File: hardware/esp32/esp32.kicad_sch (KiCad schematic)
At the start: 42 parts, among them U1 AMS1117-3.3, U2 ESP32-S3-MINI-1-N8, U3 ESD7104MUTAG, U4 BDR6133, U5 TLV75801PDRV

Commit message: TPS629210DRLR
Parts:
- removed C17, C18: 10u, Capacitor_SMD:C_0603_1608Metric, symbol Device:C
- removed C3: 100nF, Capacitor_SMD:C_0603_1608Metric, symbol Device:C
- removed C6: 10uF, Capacitor_SMD:C_0603_1608Metric, symbol Device:C_Small
- removed R8: 5.1k, Resistor_SMD:R_0603_1608Metric, symbol Device:R_Small
- removed U1: AMS1117-3.3, Package_TO_SOT_SMD:SOT-89-3, symbol Regulator_Linear:AMS1117-3.3
- removed U5: TLV75801PDRV, Package_SON:WSON-6-1EP_2x2mm_P0.65mm_EP1x1.6mm, symbol Regulator_Linear:TLV75801PDRV
- added C2, C3: 10uF, Capacitor_SMD:C_0603_1608Metric, symbol Device:C_Small
- added C5: 22uF, Capacitor_SMD:C_0603_1608Metric, symbol Device:C_Small
- added L1: 2.2uH,50mA, PCM_JLCPCB:L_0805, symbol PCM_JLCPCB-Inductors:2.2uH,50mA
- added R4: 249K, Resistor_SMD:R_0603_1608Metric, symbol Device:R_Small
- added R5: 100K, Resistor_SMD:R_0603_1608Metric, symbol Device:R_Small
- added U1: TPS629210DRLR, TPS629210DRLR:SOT50P160X60-8N, symbol TPS629210DRLR:TPS629210DRLR
- R6: value 1M -> 52.3K
- R7: value 200k -> 1K
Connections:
- net 5VUSB: now also C7.1, D1.1 (+), U4.3 (VM), C2.1, C3.1, U1.6 (VIN), U1.7 (EN)
- net GND: now also R6.1, C2.2, C3.2, C5.2, R4.1, U1.5 (GND); no longer R7.1
- net VCC: now also R7.2, C5.1, L1.2, R5.1, U1.3 (VOS); no longer C7.1, R6.2
- net at D2.2 (A): now also R7.1
- new net: R4.2, U1.1 (FB/VSET)
- new net: R5.2, U1.2 (PG)
- new net: R6.2, U1.8 (MODE/S-CONF)
- new net: L1.1, U1.4 (SW)
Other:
- moved on the sheet: C7, D2, R6, g1, g2, g3, g4

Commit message: jst
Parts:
- removed g1, g2, g3, g4, g5, g6, g7, o1, o10, o2, o3, o4, o5, o6, o7, o8, o9, tr1, tr2: TestPoint, TestPoint:TestPoint_THTPad_1.5x1.5mm_Drill0.7mm, symbol Connector:TestPoint
- added J1, J2, J3: Conn_01x02, Connector_JST:JST_SHL_SM02B-SHLS-TF_1x02-1MP_P1.00mm_Horizontal, symbol Connector_Generic:Conn_01x02
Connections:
- net GND: now also J3.1 (Pin_1), J3.2 (Pin_2)
- net at D1.3: now also J1.1 (Pin_1)
- net at D1.4: now also J1.2 (Pin_2)
- net at U4.4 (OUTA): now also J2.1 (Pin_1)
- net at U4.5 (OUTB): now also J2.2 (Pin_2)

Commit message: wip:  - ldo with ams  - ldo with TPS629210DRLR  - esp32 with usb and connectors  - tlc5940
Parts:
- added J4: Conn_01x06, Connector_JST:JST_SHL_SM06B-SHLS-TF_1x06-1MP_P1.00mm_Horizontal, symbol Connector_Generic:Conn_01x06
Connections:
- net at U2.13 (IO9): now also U4.7 (INB)
- net at U2.14 (IO10): now also U4.6 (INA)
- net at U2.16 (IO12): no longer U4.7 (INB)
- net at U2.17 (IO13): no longer U4.6 (INA)
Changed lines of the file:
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@@
 	(wire
 		(pts
-			(xy 166.37 71.12) (xy 201.93 71.12)
-		)
-		(stroke
-			(width 0)
-			(type default)
-		)
-	)
-	(wire
-		(pts
 			(xy 71.12 30.48) (xy 85.09 30.48)
 		)
@@
 	(wire
 		(pts
-			(xy 196.85 68.58) (xy 196.85 92.71)
+			(xy 196.85 60.96) (xy 196.85 92.71)
 		)
 		(stroke
@@
 	(wire
 		(pts
-			(xy 166.37 13.97) (xy 166.37 71.12)
+			(xy 166.37 13.97) (xy 166.37 63.5)
 		)
 		(stroke
@@
 	(wire
 		(pts
+			(xy 166.37 63.5) (xy 201.93 63.5)
+		)
+		(stroke
+			(width 0)
+			(type default)
+		)
+	)
+	(wire
+		(pts
 			(xy 193.04 38.1) (xy 193.04 46.99)
 		)
@@
 	(wire
 		(pts
+			(xy 196.85 60.96) (xy 201.93 60.96)
+		)
+		(stroke
+			(width 0)
+			(type default)
+		)
+	)
+	(wire
+		(pts
 			(xy 46.99 148.59) (xy 50.8 148.59)
 		)
@@
 	(wire
 		(pts
-			(xy 196.85 68.58) (xy 201.93 68.58)
-		)
-		(stroke
-			(width 0)
-			(type default)
-		)
-	)
-	(wire
-		(pts
 			(xy 50.8 175.26) (xy 48.26 175.26)
 		)
@@
 					(unit 1)
 				)
+			)
+		)
+	)
+	(symbol
+		(lib_id "Connector_Generic:Conn_01x06")
+		(at 166.37 114.3 0)
+		(unit 1)
+		(exclude_from_sim no)
+		(in_bom yes)
+		(on_board yes)
+		(dnp no)
+		(fields_autoplaced yes)
+		(property "Reference" "J4"
+			(at 168.91 114.2999 0)
+			(effects
+				(font
+					(size 1.27 1.27)
+				)
+				(justify left)
+			)
+		)
+		(property "Value" "Conn_01x06"
+			(at 168.91 116.8399 0)
+			(effects
+				(font
+					(size 1.27 1.27)
+				)
+				(justify left)
+			)
+		)
+		(property "Footprint" "Connector_JST:JST_SHL_SM06B-SHLS-TF_1x06-1MP_P1.00mm_Horizontal"
+			(at 166.37 114.3 0)
+			(effects
+				(font
+					(size 1.27 1.27)
+				)
+				(hide yes)
+			)
+		)
+		(property "Datasheet" "~"
+			(at 166.37 114.3 0)
+			(effects
+				(font
+					(size 1.27 1.27)
+				)
+				(hide yes)
+			)
+		)
+		(property "Description" "Generic connector, single row, 01x06, script generated (kicad-library-utils/schlib/autogen/connector/)"
+			(at 166.37 114.3 0)
+			(effects
+				(font
+					(size 1.27 1.27)
+				)
+				(hide yes)
+			)
+		)
+		(pin "5"
+		)
+		(pin "3"
+		)
+		(pin "4"
+		)
+		(pin "1"
+		)
+		(pin "2"
+		)
+		(pin "6"
+		)
+		(instances
+			(project ""
+				(path "/9d64b1b8-57eb-4218-8a7c-add3e4ef813a"
+					(reference "J4")
+					(unit 1)
+				)

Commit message: esp32 wip
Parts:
- removed BOOT1, RESET1: ~, Button_Switch_SMD:SW_SPST_PTS810, symbol Switch:SW_MEC_5E
- removed C1, C4: 0.1uF, Capacitor_SMD:C_0603_1608Metric, symbol Device:C_Small
- removed C2, C3, C7: 10uF, Capacitor_SMD:C_0603_1608Metric, symbol Device:C_Small
- removed C5: 22uF, Capacitor_SMD:C_0603_1608Metric, symbol Device:C_Small
- removed D1: ABS2, Diode_SMD:Diode_Bridge_Diotec_ABS, symbol Diode_Bridge:ABS2
- removed D2: LED, LED_SMD:LED_0603_1608Metric, symbol Device:LED
- removed J4: Conn_01x06, Connector_JST:JST_SHL_SM06B-SHLS-TF_1x06-1MP_P1.00mm_Horizontal, symbol Connector_Generic:Conn_01x06
- removed L1: 2.2uH,50mA, PCM_JLCPCB:L_0805, symbol PCM_JLCPCB-Inductors:2.2uH,50mA
- removed R1, R2: 5.1k, Resistor_SMD:R_0603_1608Metric, symbol Device:R_Small
- removed R3: 10k, Resistor_SMD:R_0603_1608Metric, symbol Device:R_Small
- removed R4: 249K, Resistor_SMD:R_0603_1608Metric, symbol Device:R_Small
- removed R5: 100K, Resistor_SMD:R_0603_1608Metric, symbol Device:R_Small
- removed R6: 52.3K, Resistor_SMD:R_0603_1608Metric, symbol Device:R_Small
- removed R7: 1K, Resistor_SMD:R_0603_1608Metric, symbol Device:R_Small
- removed U1: TPS629210DRLR, TPS629210DRLR:SOT50P160X60-8N, symbol TPS629210DRLR:TPS629210DRLR
- removed U3: ESD7104MUTAG, Package_DFN_QFN:Diodes_UDFN-10_1.0x2.5mm_P0.5mm, symbol Power_Protection:D3V3XA4B10LP
- removed U4: BDR6133, Library:SOIC-8-1EP_3.9x4.9mm_P1.27mm_EP2.41x3.3mm_ThermalVias, symbol RP2040-Decoder_Additional_Symbols:BDR6133
- added C2: 100n, Capacitor_SMD:C_0402_1005Metric_Pad0.74x0.62mm_HandSolder, symbol Morten_Library.kicad_sym_9:C_Small
- added C4: 1u, Capacitor_SMD:C_0603_1608Metric, symbol Morten_Library.kicad_sym_9:C_Small
- added D1: 1N5817, Diode_SMD:D_SOD-123, symbol Morten_Library.kicad_sym_9:1N5817
- added D2, D4: ESD3.3, Diode_SMD:D_SOD-923, symbol Morten_Library.kicad_sym_9:ESD9B3.3ST5G
- added F1: Polyfuse 1A, Fuse:Fuse_1206_3216Metric, symbol Morten_Library.kicad_sym_9:Polyfuse
- added FB1: BLM21PG220, Inductor_SMD:L_0805_2012Metric, symbol Morten_Library.kicad_sym_9:FerriteBead_Small
- added J4, J5, J6: Conn_01x02, Connector_JST:JST_SHL_SM02B-SHLS-TF_1x02-1MP_P1.00mm_Horizontal, symbol Connector_Generic:Conn_01x02
- added R1, R4: 5.1K, Resistor_SMD:R_0402_1005Metric, symbol Morten_Library.kicad_sym_9:R_Small
- added R2: 10K, Resistor_SMD:R_0402_1005Metric, symbol Morten_Library.kicad_sym_9:R_Small
- added SW1: RESET, Button_Switch_SMD:SW_SPST_B3U-1000P, symbol Morten_Library.kicad_sym_9:SW_SPST
- added SW2: BOOT, Button_Switch_SMD:SW_SPST_B3U-1000P, symbol Morten_Library.kicad_sym_9:SW_SPST
- added U1: USBLC6-2SC6, Package_TO_SOT_SMD:SOT-23-6, symbol Morten_Library.kicad_sym_9:USBLC6-2SC6_1
- J1, J2, J3: LCSC (none) -> C160402
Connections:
- net ESP32_EN: now also C4.1, D2.2 (A2), R2.2, SW1.2 (B)
- net GND: now also J1.1 (Pin_1), C2.2, C4.2, D2.1 (A1), D4.1 (A1), J6.2 (Pin_2), R1.2, R4.2, SW1.1 (A), SW2.1 (A), U1.2 (GND); no longer J3.1 (Pin_1), J3.2 (Pin_2)
- net GPIO0: now also D4.2 (A2), SW2.2 (B)
- net +5V: now reaches J1.2 (Pin_2)
- net +5V: now also C2.1, D1.1 (K), U1.5 (VBUS)
- net at U2.16 (IO12): now also J2.2 (Pin_2)
- net at U2.17 (IO13): now also J2.1 (Pin_1)
- net at U2.18 (IO14): now also J4.2 (Pin_2)
- net at U2.19 (IO15): now also J4.1 (Pin_1)
- net at U2.20 (IO16): now also J5.2 (Pin_2)
- net at U2.5 (IO1): now also J3.2 (Pin_2)
- net at U2.6 (IO2): now also J3.1 (Pin_1)
- net CC2: now reaches JUSB1.B5 (CC2)
- net CC2: now also R4.1
- net CC1: now reaches JUSB1.A5 (CC1)
- net CC1: now also R1.1
- net 5VUSB: no longer names the net of JUSB1.A4 (VBUS), JUSB1.A9 (VBUS), JUSB1.B4 (VBUS), JUSB1.B9 (VBUS)
- net 5VUSB: now also F1.1
- net USB_N renamed D-
- net D-: now also U1.1 (I/O1); no longer U2.23 (IO19)
- net USB_P renamed D+
- net D+: now also U1.3 (I/O2); no longer U2.24 (IO20)
- new net: D1.2 (A), FB1.2
- new net: F1.2, FB1.1
- new net +3V3: J6.1 (Pin_1), R2.1
- new net USB_D+: U1.4 (I/O2), U2.24 (IO20)
- new net USB_D-: U1.6 (I/O1), U2.23 (IO19)

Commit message: esp32
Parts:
- removed C2: 100n, Capacitor_SMD:C_0402_1005Metric_Pad0.74x0.62mm_HandSolder, symbol Morten_Library.kicad_sym_9:C_Small
- removed D1: 1N5817, Diode_SMD:D_SOD-123, symbol Morten_Library.kicad_sym_9:1N5817
- removed F1: Polyfuse 1A, Fuse:Fuse_1206_3216Metric, symbol Morten_Library.kicad_sym_9:Polyfuse
- removed FB1: BLM21PG220, Inductor_SMD:L_0805_2012Metric, symbol Morten_Library.kicad_sym_9:FerriteBead_Small
- removed J6: Conn_01x02, Connector_JST:JST_SHL_SM02B-SHLS-TF_1x02-1MP_P1.00mm_Horizontal, symbol Connector_Generic:Conn_01x02
- removed JUSB1: USB_C_Receptacle_USB2.0, Connector_USB:USB_C_Receptacle_GCT_USB4105-xx-A_16P_TopMnt_Horizontal, symbol Connector:USB_C_Receptacle_USB2.0
- removed R1, R4: 5.1K, Resistor_SMD:R_0402_1005Metric, symbol Morten_Library.kicad_sym_9:R_Small
- removed U1: USBLC6-2SC6, Package_TO_SOT_SMD:SOT-23-6, symbol Morten_Library.kicad_sym_9:USBLC6-2SC6_1
- added C18: 10u, Capacitor_SMD:C_0603_1608Metric, symbol Device:C
- added TP1, TP2: TestPoint, TestPoint:TestPoint_Pad_1.0x1.0mm, symbol Connector:TestPoint
- J2: footprint Connector_JST:JST_SHL_SM02B-SHLS-TF_1x02-1MP_P1.00mm_Horizontal -> Connector_JST:JST_ZH_S2B-ZR-SM4A-TF_1x02-1MP_P1.50mm_Horizontal; LCSC C160402 -> C157930
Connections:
- net +5V is gone; now on net USB_D+: J1.2 (Pin_2)
- net VCC is gone; now on net +3V3: U2.3 (3V3)
- net +3V3: now also J2.2 (Pin_2), C18.1
- net GND: now also J2.1 (Pin_1), C18.2; no longer J1.1 (Pin_1)
- net USB_D-: now also J1.1 (Pin_1)
- net at U2.16 (IO12): now also J3.1 (Pin_1); no longer J2.2 (Pin_2)
- net at U2.17 (IO13): now also J3.2 (Pin_2); no longer J2.1 (Pin_1)
- net at U2.18 (IO14): now also J4.1 (Pin_1); no longer J4.2 (Pin_2)
- net at U2.19 (IO15): now also J4.2 (Pin_2); no longer J4.1 (Pin_1)
- net at U2.20 (IO16): now also J5.1 (Pin_1); no longer J5.2 (Pin_2)
- net at U2.21 (IO17): now also J5.2 (Pin_2)
- net at U2.31 (IO35): now also TP1.1
- net at U2.32 (IO36): now also TP2.1
- net at U2.5 (IO1): no longer J3.2 (Pin_2)
- net at U2.6 (IO2): no longer J3.1 (Pin_1)
- no-connect marks 2 -> 0

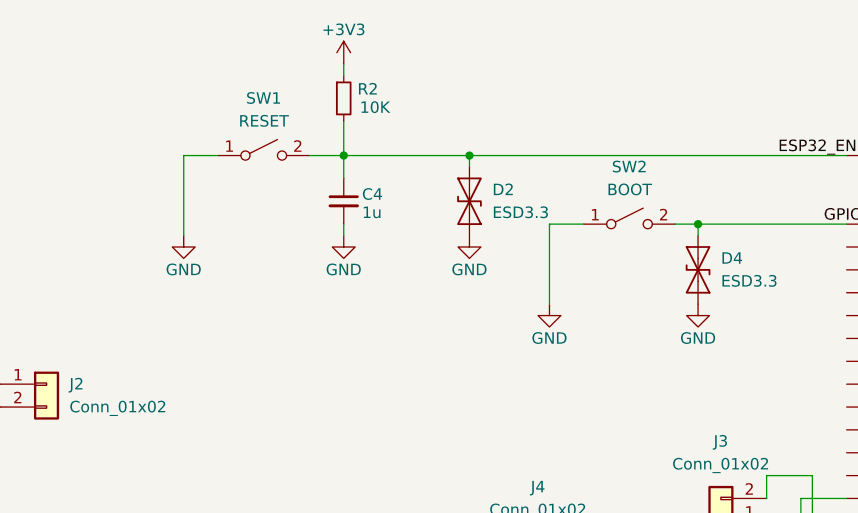
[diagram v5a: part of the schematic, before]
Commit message: simplify pins and buttons
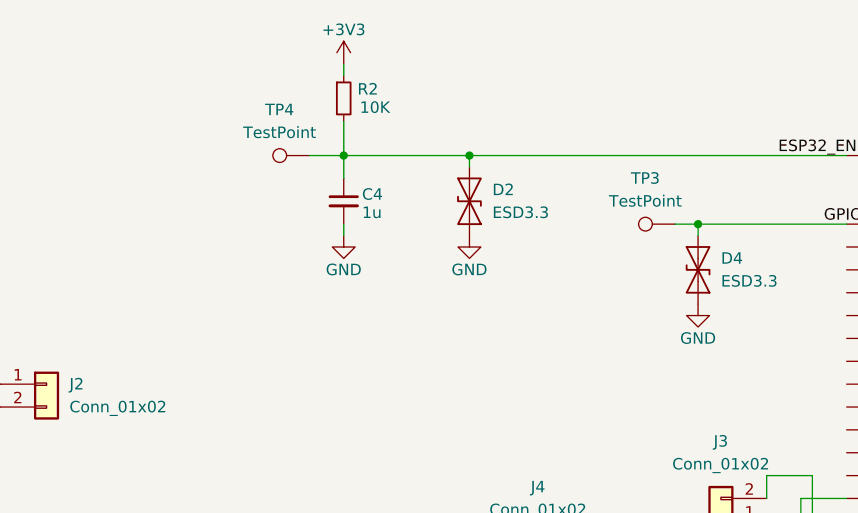
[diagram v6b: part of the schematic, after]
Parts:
- removed SW1: RESET, Button_Switch_SMD:SW_SPST_B3U-1000P, symbol Morten_Library.kicad_sym_9:SW_SPST
- removed SW2: BOOT, Button_Switch_SMD:SW_SPST_B3U-1000P, symbol Morten_Library.kicad_sym_9:SW_SPST
- added TP3, TP4: TestPoint, TestPoint:TestPoint_Pad_1.0x1.0mm, symbol Connector:TestPoint
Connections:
- net ESP32_EN: now also TP4.1
- net GPIO0: now also TP3.1
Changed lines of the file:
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@@
 	(wire
 		(pts
-			(xy 128.27 30.48) (xy 128.27 39.37)
-		)
-		(stroke
-			(width 0)
-			(type default)
-		)
-	)
-	(wire
-		(pts
 			(xy 195.58 78.74) (xy 195.58 81.28)
 		)
@@
 	(wire
 		(pts
-			(xy 172.72 38.1) (xy 168.91 38.1)
-		)
-		(stroke
-			(width 0)
-			(type default)
-		)
-	)
-	(wire
-		(pts
 			(xy 232.41 38.1) (xy 245.11 38.1)
 		)
@@
 	(wire
 		(pts
-			(xy 168.91 38.1) (xy 168.91 46.99)
-		)
-		(stroke
-			(width 0)
-			(type default)
-		)
-	)
-	(wire
-		(pts
 			(xy 193.04 66.04) (xy 193.04 68.58)
 		)
@@
 	(wire
 		(pts
-			(xy 132.08 30.48) (xy 128.27 30.48)
-		)
-		(stroke
-			(width 0)
-			(type default)
-		)
-	)
-	(wire
-		(pts
 			(xy 201.93 73.66) (xy 200.66 73.66)
 		)
@@
 	)
 	(symbol
-		(lib_id "Morten_Library.kicad_sym_9:SW_SPST")
-		(at 137.16 30.48 0)
-		(unit 1)
-		(exclude_from_sim no)
-		(in_bom yes)
-		(on_board yes)
-		(dnp no)
-		(fields_autoplaced yes)
-		(property "Reference" "SW1"
-			(at 137.16 24.13 0)
-			(effects
-				(font
-					(size 1.27 1.27)
-				)
-			)
-		)
-		(property "Value" "RESET"
-			(at 137.16 26.67 0)
-			(effects
-				(font
-					(size 1.27 1.27)
-				)
-			)
-		)
-		(property "Footprint" "Button_Switch_SMD:SW_SPST_B3U-1000P"
-			(at 137.16 30.48 0)
-			(effects
-				(font
-					(size 1.27 1.27)
-				)
-				(hide yes)
-			)
-		)
-		(property "Datasheet" "~"
-			(at 137.16 30.48 0)
-			(effects
-				(font
-					(size 1.27 1.27)
-				)
-				(hide yes)
-			)
-		)
-		(property "Description" "Single Pole Single Throw (SPST) switch"
-			(at 137.16 30.48 0)
-			(effects
-				(font
-					(size 1.27 1.27)
-				)
-				(hide yes)
-			)
-		)
-		(pin "1"
-		)
-		(pin "2"
-		)
-		(instances
-			(project "esp32"
-				(path "/9d64b1b8-57eb-4218-8a7c-add3e4ef813a"
-					(reference "SW1")
-					(unit 1)
-				)
-			)
-		)
-	)
-	(symbol
 		(lib_id "power:GND")
 		(at 232.41 116.84 90)
@@
 	)
 	(symbol
+		(lib_id "Connector:TestPoint")
+		(at 142.24 30.48 90)
+		(unit 1)
+		(exclude_from_sim no)
+		(in_bom yes)
+		(on_board yes)
+		(dnp no)
+		(fields_autoplaced yes)
+		(property "Reference" "TP4"
+			(at 138.938 25.4 90)
+			(effects
+				(font
+					(size 1.27 1.27)
+				)
+			)
+		)
+		(property "Value" "TestPoint"
+			(at 138.938 27.94 90)
+			(effects
+				(font
+					(size 1.27 1.27)
+				)
+			)
+		)
+		(property "Footprint" "TestPoint:TestPoint_Pad_1.0x1.0mm"
+			(at 142.24 25.4 0)
+			(effects
+				(font
+					(size 1.27 1.27)
+				)
+				(hide yes)
+			)
+		)
+		(property "Datasheet" "~"
+			(at 142.24 25.4 0)
+			(effects
+				(font
+					(size 1.27 1.27)
+				)
+				(hide yes)
+			)
+		)
+		(property "Description" "test point"
+			(at 142.24 30.48 0)
+			(effects
+				(font
+					(size 1.27 1.27)
+				)
+				(hide yes)
+			)
+		)
+		(pin "1"
+		)
+		(instances
+			(project "esp32"
+				(path "/9d64b1b8-57eb-4218-8a7c-add3e4ef813a"
+					(reference "TP4")
+					(unit 1)
+				)
+			)
+		)
+	)
+	(symbol
 		(lib_id "power:GND")
 		(at 232.41 88.9 90)
@@
 	)
 	(symbol
-		(lib_id "Morten_Library.kicad_sym_9:GND")
-		(at 128.27 39.37 0)
-		(unit 1)
-		(exclude_from_sim no)
-		(in_bom yes)
-		(on_board yes)
-		(dnp no)
-		(property "Reference" "#PWR040"
-			(at 128.27 45.72 0)
-			(effects
-				(font
-					(size 1.27 1.27)
-				)
-				(hide yes)
-			)
-		)
-		(property "Value" "GND"
-			(at 128.27 43.18 0)
-			(effects
-				(font
-					(size 1.27 1.27)
-				)
-			)
-		)
-		(property "Footprint" ""
-			(at 128.27 39.37 0)
-			(effects
-				(font
-					(size 1.27 1.27)
-				)
-				(hide yes)
-			)
-		)
-		(property "Datasheet" ""
-			(at 128.27 39.37 0)
-			(effects
-				(font
-					(size 1.27 1.27)
-				)
-				(hide yes)
-			)
-		)
-		(property "Description" "Power symbol creates a global label with name \"GND\" , ground"
-			(at 128.27 39.37 0)
-			(effects
-				(font
-					(size 1.27 1.27)
-				)
-				(hide yes)
-			)
-		)
-		(pin "1"
-		)
-		(instances
-			(project "esp32"
-				(path "/9d64b1b8-57eb-4218-8a7c-add3e4ef813a"
-					(reference "#PWR040")
-					(unit 1)
-				)
-			)
-		)
-	)
-	(symbol
 		(lib_id "power:GND")
 		(at 232.41 142.24 90)
@@
 	(symbol
 		(lib_id "Connector:TestPoint")
-		(at 232.41 53.34 270)
+		(at 182.88 38.1 90)
 		(unit 1)
 		(exclude_from_sim no)
@@
 		(dnp no)
 		(fields_autoplaced yes)
-		(property "Reference" "TP1"
-			(at 237.49 52.0699 90)
+		(property "Reference" "TP3"
+			(at 179.578 33.02 90)
 			(effects
 				(font
 					(size 1.27 1.27)
 				)
-				(justify left)
 			)
 		)
 		(property "Value" "TestPoint"
-			(at 237.49 54.6099 90)
+			(at 179.578 35.56 90)
 			(effects
 				(font
 					(size 1.27 1.27)
 				)
-				(justify left)
 			)
 		)
 		(property "Footprint" "TestPoint:TestPoint_Pad_1.0x1.0mm"
-			(at 232.41 58.42 0)
+			(at 182.88 33.02 0)
 			(effects
 				(font
@@
 		)
 		(property "Datasheet" "~"
-			(at 232.41 58.42 0)
+			(at 182.88 33.02 0)
 			(effects
 				(font
@@
 		)
 		(property "Description" "test point"
-			(at 232.41 53.34 0)
+			(at 182.88 38.1 0)
 			(effects
 				(font
@@
 		)
 		(instances
-			(project ""
+			(project "esp32"
 				(path "/9d64b1b8-57eb-4218-8a7c-add3e4ef813a"
-					(reference "TP1")
+					(reference "TP3")
 					(unit 1)
 				)
@@
 	)
 	(symbol
-		(lib_id "Morten_Library.kicad_sym_9:SW_SPST")
-		(at 177.8 38.1 0)
+		(lib_id "Connector:TestPoint")
+		(at 232.41 53.34 270)
 		(unit 1)
 		(exclude_from_sim no)
@@
 		(dnp no)
 		(fields_autoplaced yes)
-		(property "Reference" "SW2"
-			(at 177.8 31.75 0)
+		(property "Reference" "TP1"
+			(at 237.49 52.0699 90)
 			(effects
 				(font
 					(size 1.27 1.27)
 				)
+				(justify left)
 			)
 		)
-		(property "Value" "BOOT"
-			(at 177.8 34.29 0)
+		(property "Value" "TestPoint"
+			(at 237.49 54.6099 90)
 			(effects
 				(font
 					(size 1.27 1.27)
 				)
+				(justify left)
 			)
 		)
-		(property "Footprint" "Button_Switch_SMD:SW_SPST_B3U-1000P"
-			(at 177.8 38.1 0)
+		(property "Footprint" "TestPoint:TestPoint_Pad_1.0x1.0mm"
+			(at 232.41 58.42 0)
 			(effects
 				(font
@@
 		)
 		(property "Datasheet" "~"
-			(at 177.8 38.1 0)
+			(at 232.41 58.42 0)
 			(effects
 				(font
@@
 			)
 		)
-		(property "Description" "Single Pole Single Throw (SPST) switch"
-			(at 177.8 38.1 0)
+		(property "Description" "test point"
+			(at 232.41 53.34 0)
 			(effects
 				(font
@@
 		(pin "1"
 		)
-		(pin "2"
-		)
 		(instances
-			(project "esp32"
+			(project ""
 				(path "/9d64b1b8-57eb-4218-8a7c-add3e4ef813a"
-					(reference "SW2")
+					(reference "TP1")
 					(unit 1)
 				)
@@
 					(unit 1)
 				)
-			)
-		)
-	)
-	(symbol
-		(lib_id "Morten_Library.kicad_sym_9:GND")
-		(at 168.91 46.99 0)
-		(unit 1)
-		(exclude_from_sim no)
-		(in_bom yes)
-		(on_board yes)
-		(dnp no)
-		(property "Reference" "#PWR04"
-			(at 168.91 53.34 0)
-			(effects
-				(font
-					(size 1.27 1.27)
-				)
-				(hide yes)
-			)
-		)
-		(property "Value" "GND"
-			(at 168.91 50.8 0)
-			(effects
-				(font
-					(size 1.27 1.27)
-				)
-			)
-		)
-		(property "Footprint" ""
-			(at 168.91 46.99 0)
-			(effects
-				(font
-					(size 1.27 1.27)
-				)
-				(hide yes)
-			)
-		)
-		(property "Datasheet" ""
-			(at 168.91 46.99 0)
-			(effects
-				(font
-					(size 1.27 1.27)
-				)
-				(hide yes)
-			)
-		)
-		(property "Description" "Power symbol creates a global label with name \"GND\" , ground"
-			(at 168.91 46.99 0)
-			(effects
-				(font
-					(size 1.27 1.27)
-				)
-				(hide yes)
-			)
-		)
-		(pin "1"
-		)
-		(instances
-			(project "esp32"
-				(path "/9d64b1b8-57eb-4218-8a7c-add3e4ef813a"
-					(reference "#PWR04")
-					(unit 1)
-				)

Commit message: esp32 routing
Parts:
- removed J3, J4, J5: Conn_01x02, Connector_JST:JST_SHL_SM02B-SHLS-TF_1x02-1MP_P1.00mm_Horizontal, symbol Connector_Generic:Conn_01x02
- removed TP1, TP2: TestPoint, TestPoint:TestPoint_Pad_1.0x1.0mm, symbol Connector:TestPoint
- added J6: Conn_01x08, Connector_JST:JST_SHL_SM08B-SHLS-TF_1x08-1MP_P1.00mm_Horizontal, symbol Connector_Generic:Conn_01x08
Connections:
- net at U2.15 (IO11): now also J6.1 (Pin_1)
- net at U2.16 (IO12): now also J6.2 (Pin_2)
- net at U2.17 (IO13): now also J6.3 (Pin_3)
- net at U2.18 (IO14): now also J6.4 (Pin_4)
- net at U2.19 (IO15): now also J6.5 (Pin_5)
- net at U2.20 (IO16): now also J6.6 (Pin_6)
- net at U2.21 (IO17): now also J6.7 (Pin_7)
- net at U2.22 (IO18): now also J6.8 (Pin_8)

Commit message: esp32
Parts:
- added TP1: TestPoint, MountingHole:MountingHole_2.1mm, symbol Connector:TestPoint
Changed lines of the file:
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@@
+	)
+	(symbol
+		(lib_id "Connector:TestPoint")
+		(at 73.66 163.83 180)
+		(unit 1)
+		(exclude_from_sim no)
+		(in_bom yes)
+		(on_board yes)
+		(dnp no)
+		(fields_autoplaced yes)
+		(property "Reference" "TP1"
+			(at 76.2 165.8619 0)
+			(effects
+				(font
+					(size 1.27 1.27)
+				)
+				(justify right)
+			)
+		)
+		(property "Value" "TestPoint"
+			(at 76.2 168.4019 0)
+			(effects
+				(font
+					(size 1.27 1.27)
+				)
+				(justify right)
+			)
+		)
+		(property "Footprint" "MountingHole:MountingHole_2.1mm"
+			(at 68.58 163.83 0)
+			(effects
+				(font
+					(size 1.27 1.27)
+				)
+				(hide yes)
+			)
+		)
+		(property "Datasheet" "~"
+			(at 68.58 163.83 0)
+			(effects
+				(font
+					(size 1.27 1.27)
+				)
+				(hide yes)
+			)
+		)
+		(property "Description" "test point"
+			(at 73.66 163.83 0)
+			(effects
+				(font
+					(size 1.27 1.27)
+				)
+				(hide yes)
+			)
+		)
+		(pin "1"
+		)
+		(instances
+			(project "esp32"
+				(path "/9d64b1b8-57eb-4218-8a7c-add3e4ef813a"
+					(reference "TP1")
+					(unit 1)
+				)
+			)
+		)
 	)
 	(symbol
